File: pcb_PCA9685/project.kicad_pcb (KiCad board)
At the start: 4 copper layers, 18.3 x 25.9 mm, 47 parts, among them IC1 PCA9685PW,118

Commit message: Add revision number to PCB
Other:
- board text added: "Rev.: ${REVISION}"
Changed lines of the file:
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@@
 	(paper "A4")
 	(title_block
-		(comment 4 "AISLER Project ID: UBKWEFRY")
+		(title "Breakout board: IO-Expander based on PCA9685")
+		(date "2024-06-09")
+		(rev "1")
+		(company "Thomas Fanninger")
 	)
 	(layers
@@
 			)
 			(justify left bottom mirror)
+		)
+	)
+	(gr_text "Rev.: ${REVISION}"
+		(at 112.014 103.632 0)
+		(layer "B.SilkS")
+		(effects
+			(font
+				(size 0.6 0.6)
+				(thickness 0.1)
+				(bold yes)
+			)
+			(justify left bottom mirror)

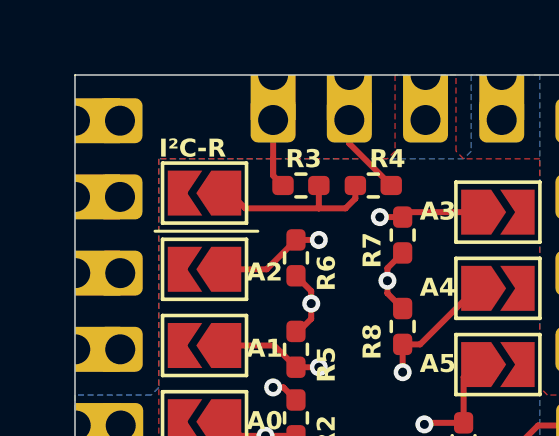
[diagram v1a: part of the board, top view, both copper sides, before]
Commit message: Correct kibot for four layer
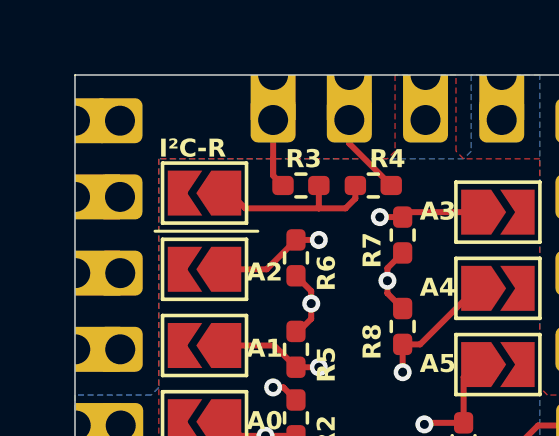
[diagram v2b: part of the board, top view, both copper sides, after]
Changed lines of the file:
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@@
 			(outputformat 1)
 			(mirror no)
-			(drillshape 1)
+			(drillshape 0)
 			(scaleselection 1)
-			(outputdirectory "")
+			(outputdirectory "../../../../test/")
 		)
 	)
@@
 		(pad "1" thru_hole rect
 			(at 0 0)
-			(size 1.5 1.5)
+			(size 0.9398 1.5)
 			(drill 1
-				(offset 0.75 0)
+				(offset 0.4699 0)
 			)
 			(property pad_prop_castellated)
@@
 		(pad "1" thru_hole roundrect
 			(at 1.5 0)
-			(size 1.5 1.5)
-			(drill 1)
+			(size 1.615 1.5)
+			(drill 1
+				(offset -0.0575 0)
+			)
 			(property pad_prop_castellated)
 			(layers "*.Cu" "*.Mask")
@@
 			)
 		)
-		(property "LCSC#" " C2678753"
-			(at 0 0 0)
-			(unlocked yes)
+		(property "LCSC#" "C2678753"
+			(at 0 0 0)
+			(unlocked yes)

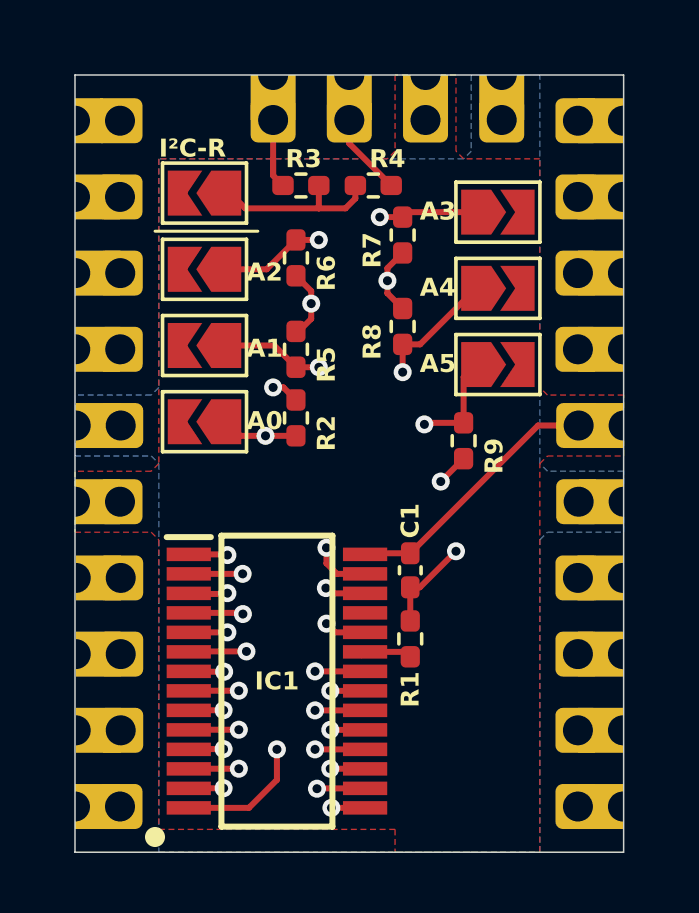
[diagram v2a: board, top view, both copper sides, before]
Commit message: Correct kibot for four layer
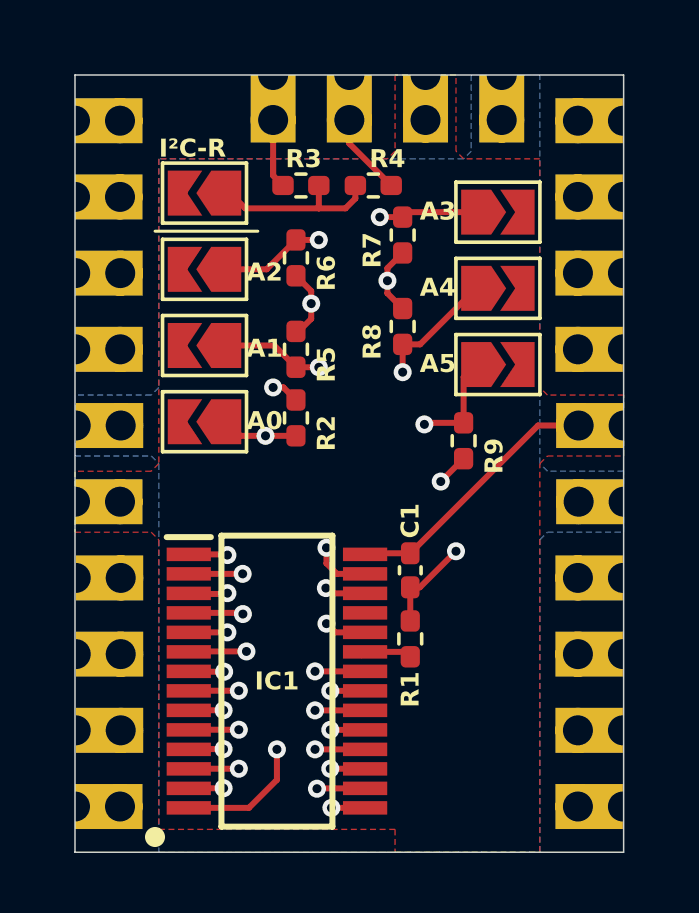
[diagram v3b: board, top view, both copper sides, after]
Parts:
- removed REF** (x4): Tab, kikit:Tab
- added T1: Tab, PCM_kikit:Tab, F.Cu at (97.8, 78.0)
- added T2: Tab, PCM_kikit:Tab, F.Cu at (113.5, 78.0)
- added T3: Tab, PCM_kikit:Tab, F.Cu at (97.8, 104.4)
- added T4: Tab, PCM_kikit:Tab, F.Cu at (113.5, 104.4)
